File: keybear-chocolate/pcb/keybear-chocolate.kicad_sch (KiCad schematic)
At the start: 95 parts, among them J1 MJ-4PP-9, J2 BATT, J3 LED, J4 OLED, SW1 SW_PUSH, SW10 SW_PUSH, SW11 SW_PUSH, SW12 SW_PUSH, SW13 SW_PUSH, SW14 SW_PUSH, SW15 SW_PUSH, SW16 SW_PUSH, SW17 SW_PUSH, SW18 SW_PUSH, SW19 SW_PUSH, SW2 SW_PUSH, SW20 SW_PUSH, SW21 SW_PUSH, SW22 SW_PUSH, SW23 SW_PUSH, SW25 Rotary_Encoder_Switch, SW3 SW_PUSH, SW30 BATT_SW, SW4 SW_PUSH, SW5 SW_PUSH, SW6 SW_PUSH, SW7 SW_PUSH, SW8 SW_PUSH, SW9 SW_PUSH, U1 ProMicro

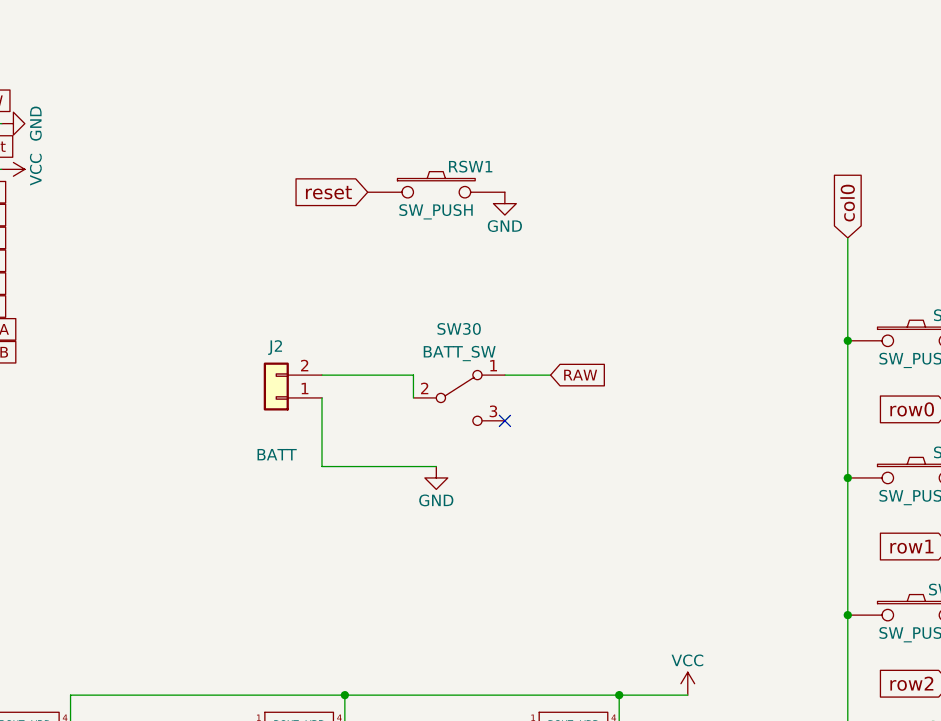
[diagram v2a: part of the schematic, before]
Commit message: adding holes to the pcb
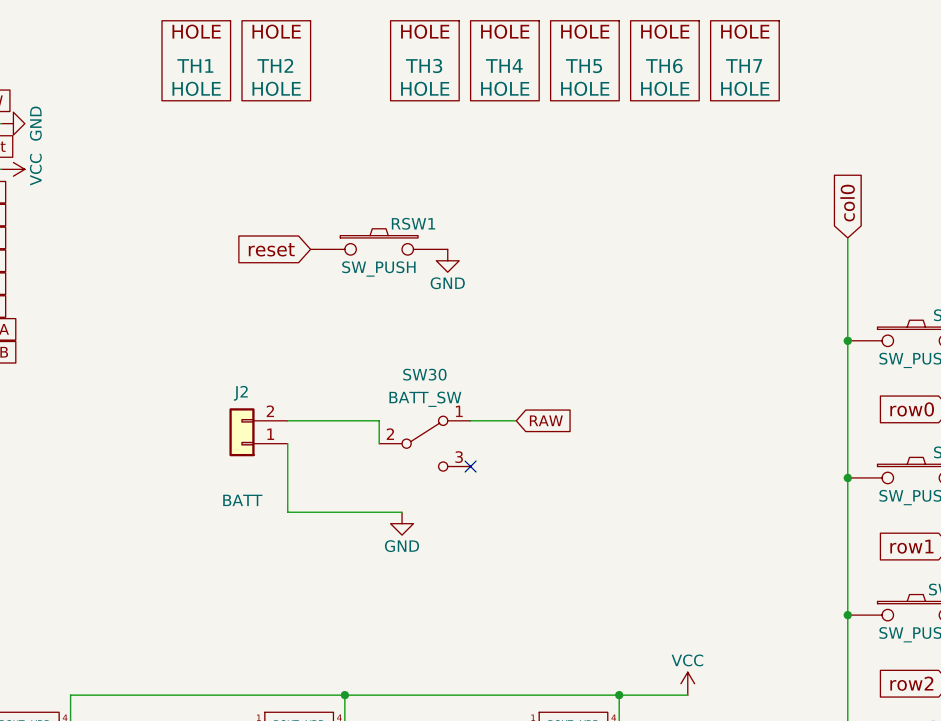
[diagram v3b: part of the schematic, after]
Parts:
- added TH1, TH2: HOLE, SofleKeyboard-footprint:M2_HOLE_PCB, symbol SofleKeyboard-rescue:HOLE-Lily58-cache-Lily58_Pro-rescue
- added TH3, TH4, TH5, TH6, TH7: HOLE, SofleKeyboard-footprint:HOLE_M2_TH, symbol SofleKeyboard-rescue:HOLE-Lily58-cache-Lily58_Pro-rescue
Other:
- moved on the sheet: J2, RSW1, SW30

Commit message: holes added
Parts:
- removed TH1, TH2: HOLE, SofleKeyboard-footprint:M2_HOLE_PCB, symbol SofleKeyboard-rescue:HOLE-Lily58-cache-Lily58_Pro-rescue
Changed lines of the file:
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@@
-    )
-  )
-  (symbol (lib_id "SofleKeyboard-rescue:HOLE-Lily58-cache-Lily58_Pro-rescue") (at 91.44 20.32 0) (unit 1)
-    (in_bom yes) (on_board yes) (dnp no)
-    (property "Reference" "TH1" (at 91.44 20.32 0)
-      (effects (font (size 1.524 1.524)))
-    )
-    (property "Value" "HOLE" (at 91.44 22.86 0)
-      (effects (font (size 1.524 1.524)))
-    )
-    (property "Footprint" "SofleKeyboard-footprint:M2_HOLE_PCB" (at 91.44 20.32 0)
-      (effects (font (size 1.524 1.524)) hide)
-    )
-    (property "Datasheet" "" (at 91.44 20.32 0)
-      (effects (font (size 1.524 1.524)))
-    )
-    (instances
-      (project "SofleKeyboard"
-        (path "/806aebb6-fec4-4c01-9a5d-54b967a9cf68"
-          (reference "TH1") (unit 1)
-        )
-      )
-      (project "keybear-chocolate"
-        (path "/b2404ab0-025a-473e-9fbb-0abc932972cf"
-          (reference "TH1") (unit 1)
-        )
-      )
     )
   )
@@
         )
       )
-    )
-  )
-  (symbol (lib_id "SofleKeyboard-rescue:HOLE-Lily58-cache-Lily58_Pro-rescue") (at 100.33 20.32 0) (unit 1)
-    (in_bom yes) (on_board yes) (dnp no)
-    (property "Reference" "TH2" (at 100.33 20.32 0)
-      (effects (font (size 1.524 1.524)))
-    )
-    (property "Value" "HOLE" (at 100.33 22.86 0)
-      (effects (font (size 1.524 1.524)))
-    )
-    (property "Footprint" "SofleKeyboard-footprint:M2_HOLE_PCB" (at 100.33 20.32 0)
-      (effects (font (size 1.524 1.524)) hide)
-    )
-    (property "Datasheet" "" (at 100.33 20.32 0)
-      (effects (font (size 1.524 1.524)))
-    )
-    (instances
-      (project "SofleKeyboard"
-        (path "/806aebb6-fec4-4c01-9a5d-54b967a9cf68"
-          (reference "TH2") (unit 1)
-        )
-      )
-      (project "keybear-chocolate"
-        (path "/b2404ab0-025a-473e-9fbb-0abc932972cf"
-          (reference "TH2") (unit 1)
-        )
-      )

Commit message: updated diode, fixed ground filled layer and other small fixes
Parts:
- D2: footprint kbd:D3_SMD_v2 -> kbd:D3_SMD
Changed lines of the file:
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@@
       (effects (font (size 1.27 1.27)))
     )
-    (property "Footprint" "kbd:D3_SMD_v2" (at 196.85 54.61 0)
+    (property "Footprint" "kbd:D3_SMD" (at 196.85 54.61 0)
       (effects (font (size 1.27 1.27)) hide)
     )

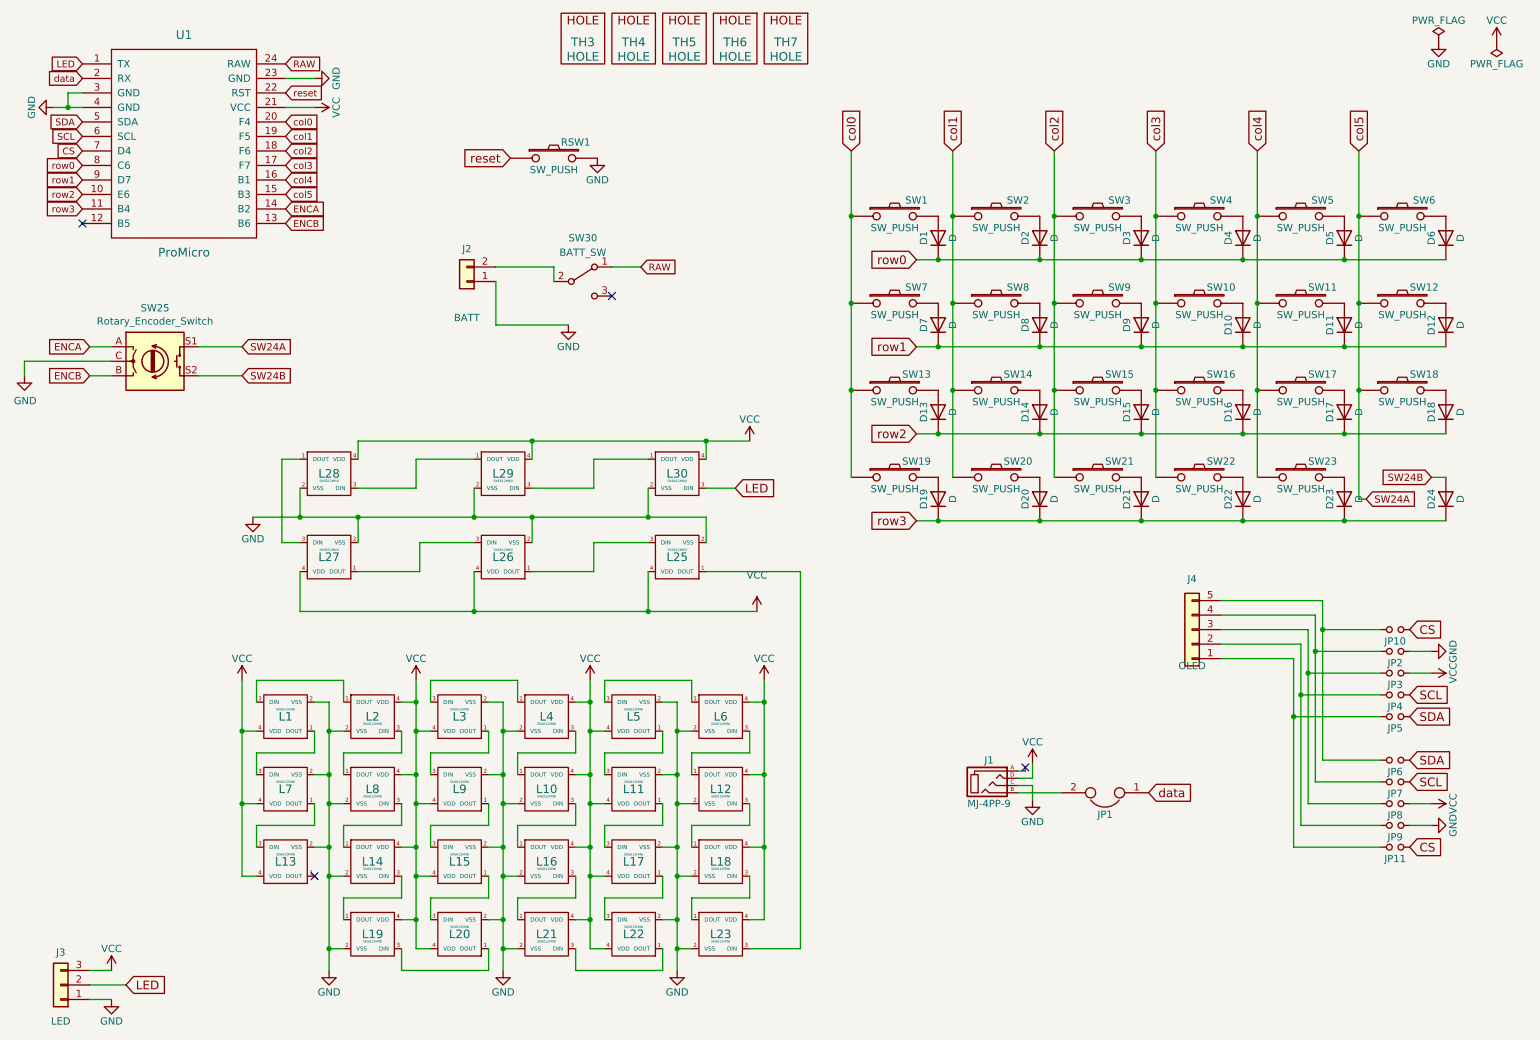
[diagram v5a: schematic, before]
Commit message: resistors added back
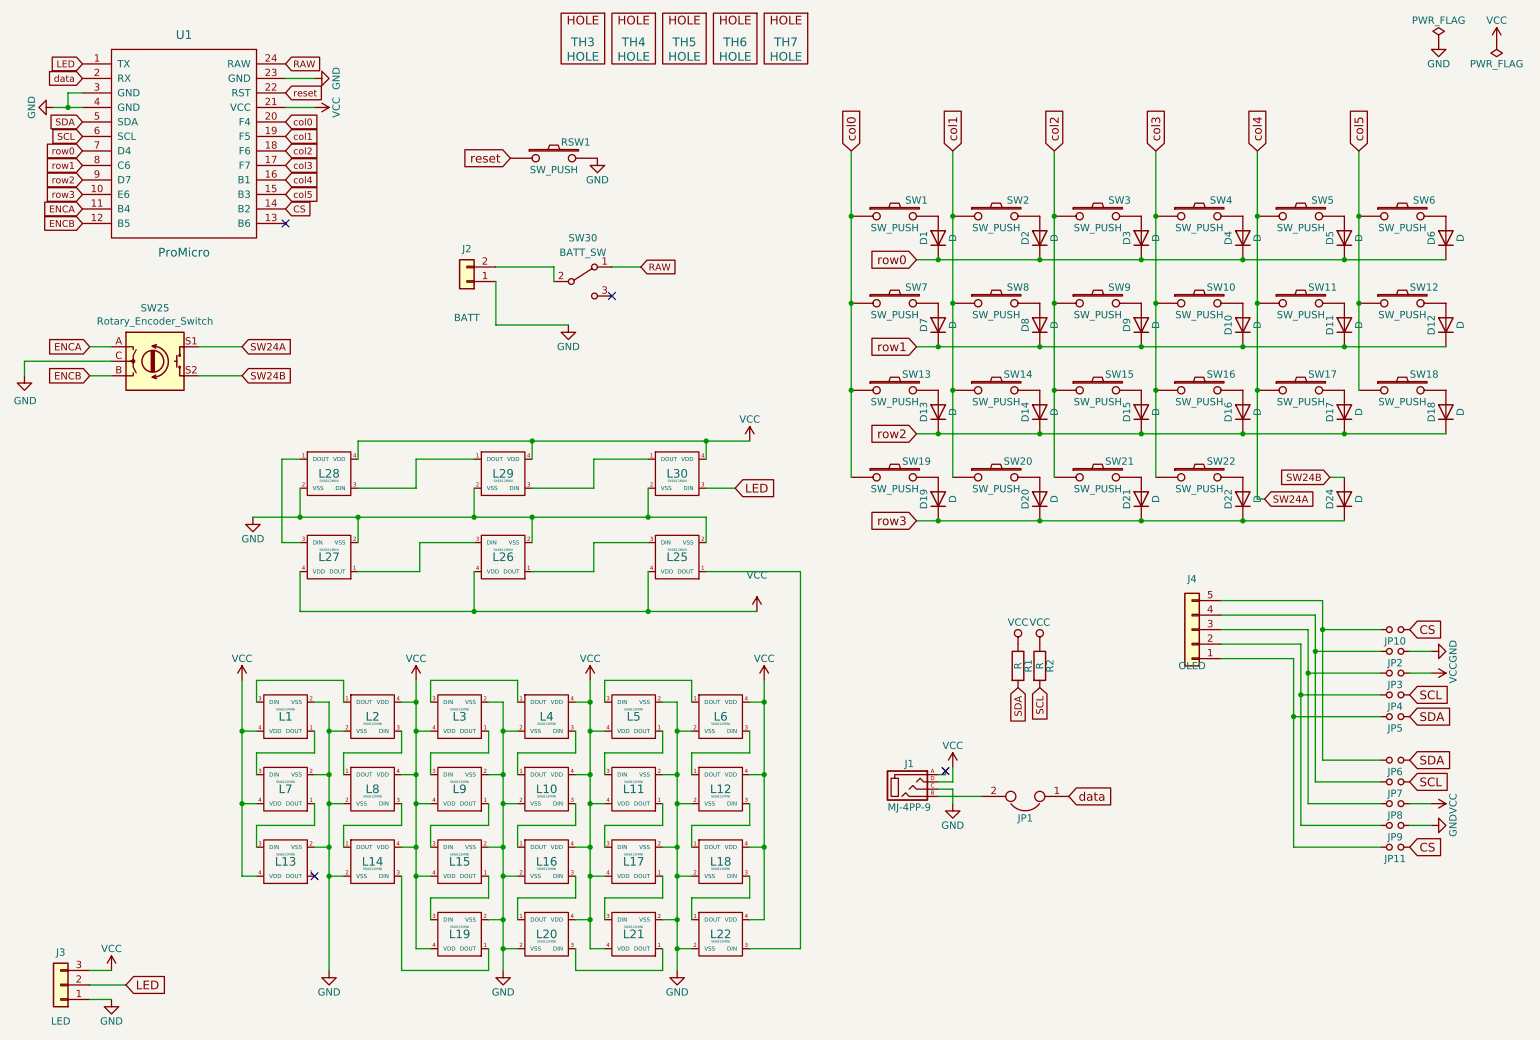
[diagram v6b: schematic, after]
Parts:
- removed D23: D, kbd:D3_SMD, symbol Device:D
- removed L19: SK6812MINI, kbd:SK6812MINI_xo_v02, symbol corne-chocolate-rescue:SK6812MINI-kbd
- removed SW23: SW_PUSH, kbd:Choc_Hotswap_1.5u, symbol corne-chocolate-rescue:SW_PUSH-kbd
- added R1, R2: R, SofleKeyboard-footprint:RESISTOR_mini, symbol SofleKeyboard-rescue:R-Lily58-cache-Lily58_Pro-rescue
- renumbered L20 to L19, L21 to L20, L22 to L21, L23 to L22
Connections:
- net col4 is gone; now on net SW24A: SW11.1, SW17.1, SW5.1, U1.16 (B1)
- net CS: now also U1.14 (B2); no longer U1.7 (D4)
- net ENCA: now also U1.11 (B4); no longer U1.14 (B2)
- net ENCB: now also U1.12 (B5); no longer U1.13 (B6)
- net SCL: now also R2.2
- net SDA: now also R1.2
- net SW24A: no longer SW12.1, SW18.1, SW6.1, U1.15 (B3)
- net VCC: now also R1.1, R2.1
- net row0: now also U1.7 (D4); no longer U1.8 (C6)
- net row1: now also U1.8 (C6); no longer U1.9 (D7)
- net row2: now also U1.9 (D7); no longer U1.10 (E6)
- net row3: now also U1.10 (E6); no longer U1.11 (B4)
- net at L14.3 (DIN): now also L19.1 (DOUT)
- new net col5: SW12.1, SW18.1, SW6.1, U1.15 (B3)
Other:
- moved on the sheet: D24, J1, JP1

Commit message: moving LED ping. Adding/rename RX/TX
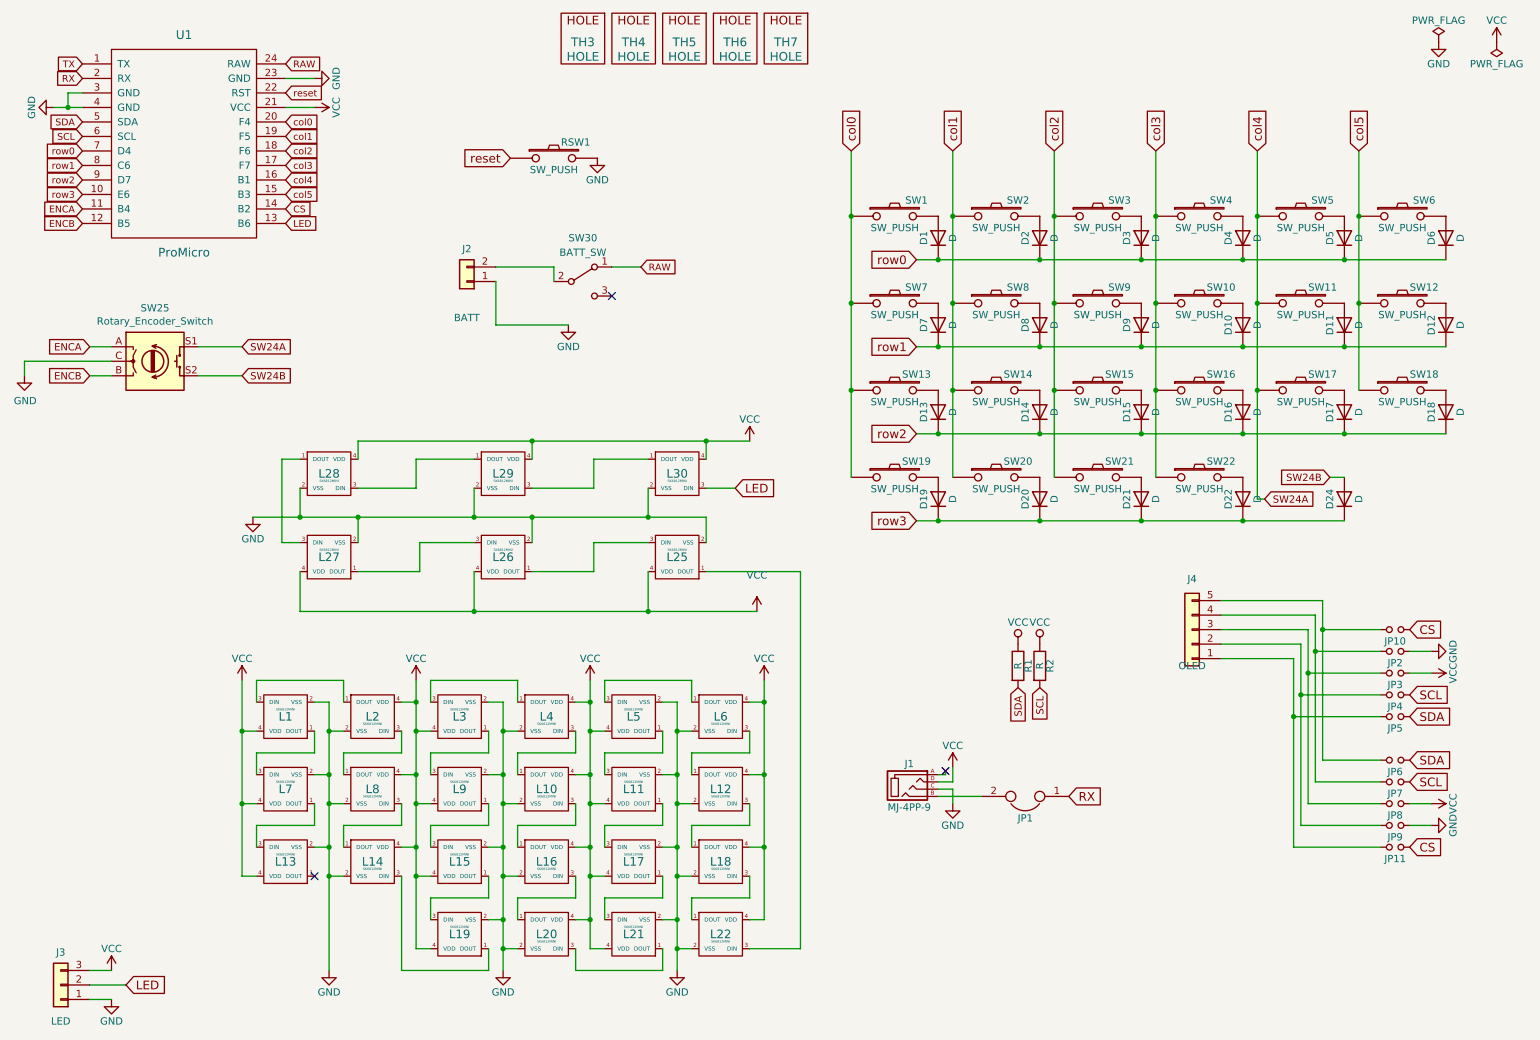
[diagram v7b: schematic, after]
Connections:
- net LED: now also U1.13 (B6); no longer U1.1 (TX)
- net data renamed RX
- new net TX: U1.1 (TX)
- no-connect marks 4 -> 3
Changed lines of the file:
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@@
   (no_connect (at 180.34 147.955))
   (no_connect (at 121.92 64.77))
-  (no_connect (at 64.77 52.07))
   (no_connect (at 69.85 166.37))
   (wire (pts (xy 180.34 148.59) (xy 179.07 148.59))
@@
     )
   )
-  (global_label "data" (shape input) (at 29.21 26.67 180) (fields_autoplaced)
+  (global_label "RX" (shape input) (at 29.21 26.67 180) (fields_autoplaced)
     (effects (font (size 1.1938 1.1938)) (justify right))
-    (property "Intersheetrefs" "${INTERSHEET_REFS}" (at 23.0966 26.67 0)
+    (property "Intersheetrefs" "${INTERSHEET_REFS}" (at 24.6883 26.67 0)
       (effects (font (size 1.27 1.27)) (justify right) hide)
     )
@@
     )
   )
-  (global_label "data" (shape input) (at 201.93 152.4 0) (fields_autoplaced)
+  (global_label "RX" (shape input) (at 201.93 152.4 0) (fields_autoplaced)
     (effects (font (size 1.524 1.524)) (justify left))
-    (property "Intersheetrefs" "${INTERSHEET_REFS}" (at 209.7344 152.4 0)
+    (property "Intersheetrefs" "${INTERSHEET_REFS}" (at 207.7022 152.4 0)
       (effects (font (size 1.27 1.27)) (justify left) hide)
     )
@@
     )
   )
-  (global_label "LED" (shape input) (at 29.21 24.13 180) (fields_autoplaced)
+  (global_label "TX" (shape input) (at 29.21 24.13 180) (fields_autoplaced)
     (effects (font (size 1.1938 1.1938)) (justify right))
-    (property "Intersheetrefs" "${INTERSHEET_REFS}" (at 23.7788 24.13 0)
+    (property "Intersheetrefs" "${INTERSHEET_REFS}" (at 24.9725 24.13 0)
       (effects (font (size 1.27 1.27)) (justify right) hide)
     )
@@
     )
   )
+  (global_label "LED" (shape input) (at 64.77 52.07 0) (fields_autoplaced)
+    (effects (font (size 1.1938 1.1938)) (justify left))
+    (property "Intersheetrefs" "${INTERSHEET_REFS}" (at 70.2012 52.07 0)
+      (effects (font (size 1.27 1.27)) (justify left) hide)
+    )
+  )
